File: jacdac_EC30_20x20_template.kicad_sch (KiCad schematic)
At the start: 6 parts

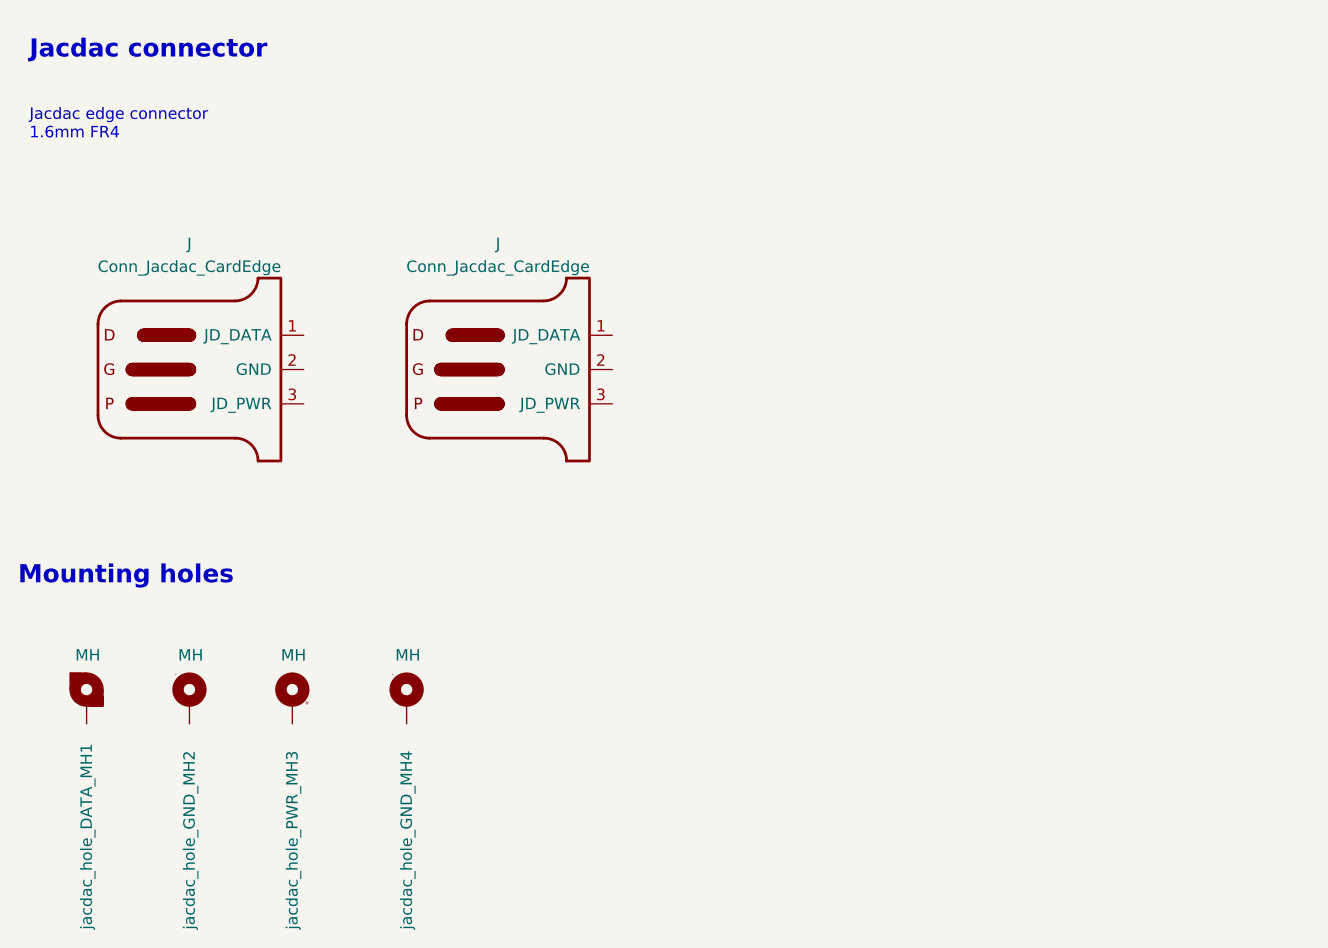
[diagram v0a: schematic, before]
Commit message: Board and schematic v0.0 ready for review
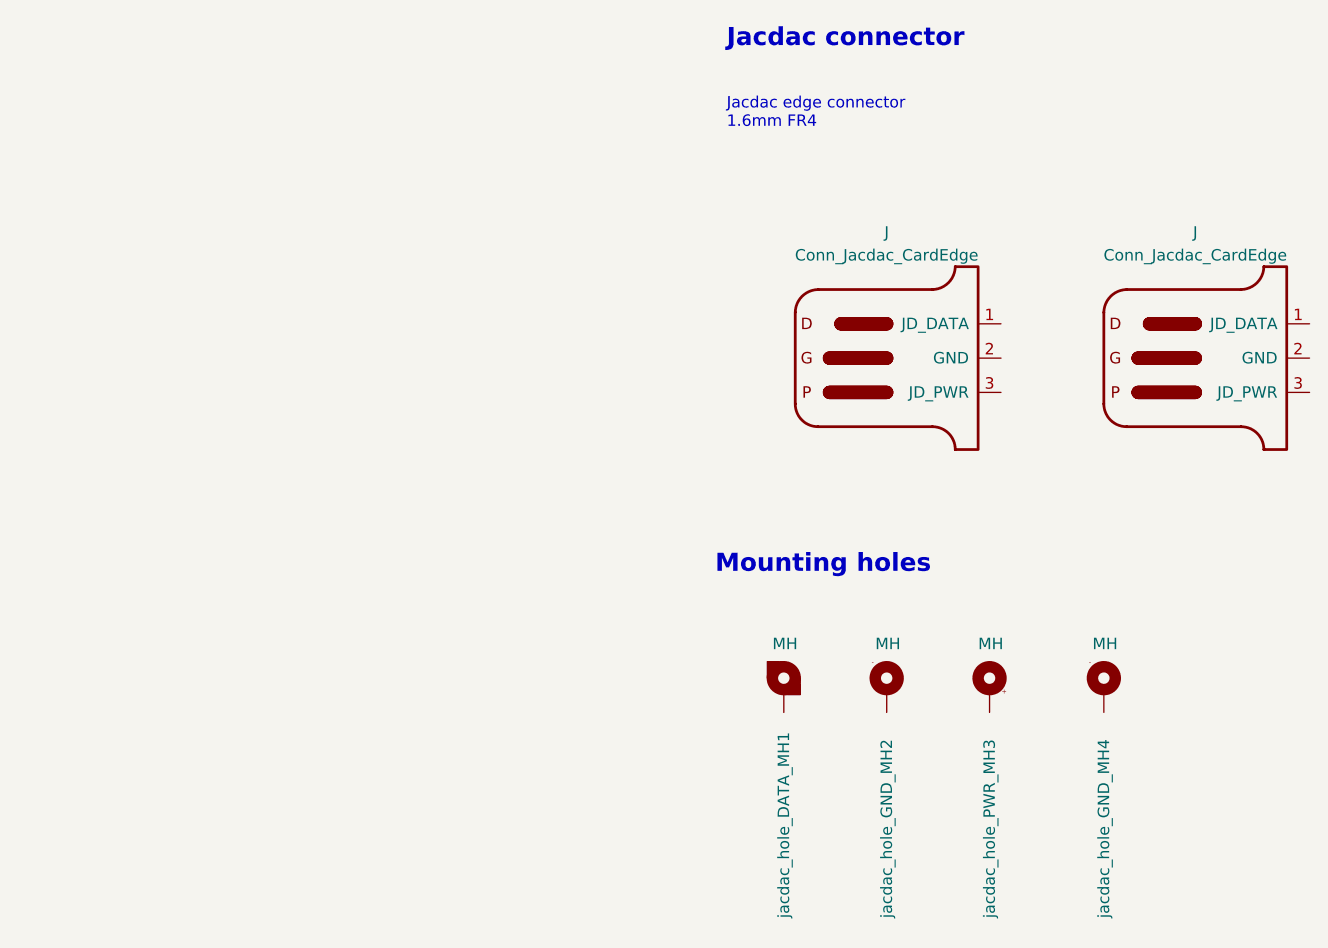
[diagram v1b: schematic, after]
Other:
- moved on the sheet: J, MH
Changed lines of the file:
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@@
     (comment 3 "Conforms to: \"EC\" template: 20x20mm MH, 1 + 1 conns v1.0")
   )
-  (text "Jacdac connector" (at 35.56 48.26 0)
+  (text "Jacdac connector" (at 113.03 46.99 0)
     (effects (font (size 2.0066 2.0066) (thickness 0.4013) bold) (justify left bottom))
   )
-  (text "Mounting holes" (at 34.29 106.68 0)
+  (text "Mounting holes" (at 111.76 105.41 0)
     (effects (font (size 2.0066 2.0066) (thickness 0.4013) bold) (justify left bottom))
   )
-  (text "Jacdac edge connector\n1.6mm FR4" (at 35.56 57.15 0)
+  (text "Jacdac edge connector\n1.6mm FR4" (at 113.03 55.88 0)
     (effects (font (size 1.27 1.27)) (justify left bottom))
   )
-  (symbol (lib_id "Jacdac:Conn_Jacdac_CardEdge") (at 88.9 82.55 0) (unit 1)
+  (symbol (lib_id "Jacdac:Conn_Jacdac_CardEdge") (at 166.37 81.28 0) (unit 1)
     (in_bom no) (on_board yes) (fields_autoplaced)
     (default_instance (reference "J") (unit 1) (value "Conn_Jacdac_CardEdge") (footprint "Jacdac:JD-PEC-02_Prerouted_recessed"))
-    (property "Reference" "J" (id 0) (at 87.6299 68.58 0)
+    (property "Reference" "J" (id 0) (at 165.0999 67.31 0)
       (effects (font (size 1.27 1.27)))
     )
-    (property "Value" "Conn_Jacdac_CardEdge" (id 1) (at 87.6299 71.12 0)
+    (property "Value" "Conn_Jacdac_CardEdge" (id 1) (at 165.0999 69.85 0)
       (effects (font (size 1.27 1.27)))
     )
-    (property "Footprint" "Jacdac:JD-PEC-02_Prerouted_recessed" (id 2) (at 93.98 93.98 0)
+    (property "Footprint" "Jacdac:JD-PEC-02_Prerouted_recessed" (id 2) (at 171.45 92.71 0)
       (effects (font (size 1.27 1.27)) hide)
     )
-    (property "Datasheet" "" (id 3) (at 80.01 114.3 90)
+    (property "Datasheet" "" (id 3) (at 157.48 113.03 90)
       (effects (font (size 1.27 1.27)) hide)
     )
@@
     (pin "3")
   )
-  (symbol (lib_id "Jacdac:jacdac_hole_PWR_MH3") (at 64.77 119.38 0) (unit 1)
+  (symbol (lib_id "Jacdac:jacdac_hole_PWR_MH3") (at 142.24 118.11 0) (unit 1)
     (in_bom no) (on_board yes)
     (default_instance (reference "MH") (unit 1) (value "jacdac_hole_PWR_MH3") (footprint "Jacdac:jacdac_hole_PWR_MH3"))
-    (property "Reference" "MH" (id 0) (at 63.5 114.3 0)
+    (property "Reference" "MH" (id 0) (at 140.97 113.03 0)
       (effects (font (size 1.27 1.27)) (justify left))
     )
-    (property "Value" "jacdac_hole_PWR_MH3" (id 1) (at 64.77 144.78 90)
+    (property "Value" "jacdac_hole_PWR_MH3" (id 1) (at 142.24 143.51 90)
       (effects (font (size 1.27 1.27)) (justify left))
     )
-    (property "Footprint" "Jacdac:jacdac_hole_PWR_MH3" (id 2) (at 64.77 127 0)
+    (property "Footprint" "Jacdac:jacdac_hole_PWR_MH3" (id 2) (at 142.24 125.73 0)
       (effects (font (size 1.27 1.27)) hide)
     )
-    (property "Datasheet" "" (id 3) (at 64.77 118.11 0)
+    (property "Datasheet" "" (id 3) (at 142.24 116.84 0)
       (effects (font (size 0 0)) hide)
     )
     (pin "MH3")
   )
-  (symbol (lib_id "Jacdac:Conn_Jacdac_CardEdge") (at 54.61 82.55 0) (unit 1)
+  (symbol (lib_id "Jacdac:Conn_Jacdac_CardEdge") (at 132.08 81.28 0) (unit 1)
     (in_bom no) (on_board yes) (fields_autoplaced)
     (default_instance (reference "J") (unit 1) (value "Conn_Jacdac_CardEdge") (footprint "Jacdac:JD-PEC-02_Prerouted_recessed"))
-    (property "Reference" "J" (id 0) (at 53.3399 68.58 0)
+    (property "Reference" "J" (id 0) (at 130.8099 67.31 0)
       (effects (font (size 1.27 1.27)))
     )
-    (property "Value" "Conn_Jacdac_CardEdge" (id 1) (at 53.3399 71.12 0)
+    (property "Value" "Conn_Jacdac_CardEdge" (id 1) (at 130.8099 69.85 0)
       (effects (font (size 1.27 1.27)))
     )
-    (property "Footprint" "Jacdac:JD-PEC-02_Prerouted_recessed" (id 2) (at 59.69 93.98 0)
+    (property "Footprint" "Jacdac:JD-PEC-02_Prerouted_recessed" (id 2) (at 137.16 92.71 0)
       (effects (font (size 1.27 1.27)) hide)
     )
-    (property "Datasheet" "" (id 3) (at 45.72 114.3 90)
+    (property "Datasheet" "" (id 3) (at 123.19 113.03 90)
       (effects (font (size 1.27 1.27)) hide)
     )
@@
     (pin "3")
   )
-  (symbol (lib_id "Jacdac:jacdac_hole_DATA_MH1") (at 41.91 119.38 0) (unit 1)
+  (symbol (lib_id "Jacdac:jacdac_hole_DATA_MH1") (at 119.38 118.11 0) (unit 1)
     (in_bom no) (on_board yes)
     (default_instance (reference "MH") (unit 1) (value "jacdac_hole_DATA_MH1") (footprint "Jacdac:jacdac_hole_DATA_notched_MH1"))
-    (property "Reference" "MH" (id 0) (at 40.64 114.3 0)
+    (property "Reference" "MH" (id 0) (at 118.11 113.03 0)
       (effects (font (size 1.27 1.27)) (justify left))
     )
-    (property "Value" "jacdac_hole_DATA_MH1" (id 1) (at 41.91 144.78 90)
+    (property "Value" "jacdac_hole_DATA_MH1" (id 1) (at 119.38 143.51 90)
       (effects (font (size 1.27 1.27)) (justify left))
     )
-    (property "Footprint" "Jacdac:jacdac_hole_DATA_notched_MH1" (id 2) (at 41.91 126.746 0)
+    (property "Footprint" "Jacdac:jacdac_hole_DATA_notched_MH1" (id 2) (at 119.38 125.476 0)
       (effects (font (size 1.27 1.27)) hide)
     )
-    (property "Datasheet" "" (id 3) (at 41.91 118.11 0)
+    (property "Datasheet" "" (id 3) (at 119.38 116.84 0)
       (effects (font (size 0 0)) hide)
     )
     (pin "MH1")
   )
-  (symbol (lib_id "Jacdac:jacdac_hole_GND_MH2") (at 53.34 119.38 0) (unit 1)
+  (symbol (lib_id "Jacdac:jacdac_hole_GND_MH2") (at 130.81 118.11 0) (unit 1)
     (in_bom no) (on_board yes)
     (default_instance (reference "MH") (unit 1) (value "jacdac_hole_GND_MH2") (footprint "Jacdac:jacdac_hole_GND_MH2"))
-    (property "Reference" "MH" (id 0) (at 52.07 114.3 0)
+    (property "Reference" "MH" (id 0) (at 129.54 113.03 0)
       (effects (font (size 1.27 1.27)) (justify left))
     )
-    (property "Value" "jacdac_hole_GND_MH2" (id 1) (at 53.34 144.78 90)
+    (property "Value" "jacdac_hole_GND_MH2" (id 1) (at 130.81 143.51 90)
       (effects (font (size 1.27 1.27)) (justify left))
     )
-    (property "Footprint" "Jacdac:jacdac_hole_GND_MH2" (id 2) (at 53.34 126.746 0)
+    (property "Footprint" "Jacdac:jacdac_hole_GND_MH2" (id 2) (at 130.81 125.476 0)
       (effects (font (size 1.27 1.27)) hide)
     )
-    (property "Datasheet" "" (id 3) (at 53.34 118.11 0)
+    (property "Datasheet" "" (id 3) (at 130.81 116.84 0)
       (effects (font (size 0 0)) hide)
     )
     (pin "MH2")
   )
-  (symbol (lib_id "Jacdac:jacdac_hole_GND_MH4") (at 77.47 119.38 0) (unit 1)
+  (symbol (lib_id "Jacdac:jacdac_hole_GND_MH4") (at 154.94 118.11 0) (unit 1)
     (in_bom no) (on_board yes)
     (default_instance (reference "MH") (unit 1) (value "jacdac_hole_GND_MH4") (footprint "Jacdac:jacdac_hole_GND_MH4"))
-    (property "Reference" "MH" (id 0) (at 76.2 114.3 0)
+    (property "Reference" "MH" (id 0) (at 153.67 113.03 0)
       (effects (font (size 1.27 1.27)) (justify left))
     )
-    (property "Value" "jacdac_hole_GND_MH4" (id 1) (at 77.47 144.78 90)
+    (property "Value" "jacdac_hole_GND_MH4" (id 1) (at 154.94 143.51 90)
       (effects (font (size 1.27 1.27)) (justify left))
     )
-    (property "Footprint" "Jacdac:jacdac_hole_GND_MH4" (id 2) (at 77.47 126.746 0)
+    (property "Footprint" "Jacdac:jacdac_hole_GND_MH4" (id 2) (at 154.94 125.476 0)
       (effects (font (size 1.27 1.27)) hide)
     )
-    (property "Datasheet" "" (id 3) (at 77.47 118.11 0)
+    (property "Datasheet" "" (id 3) (at 154.94 116.84 0)
       (effects (font (size 0 0)) hide)
     )
